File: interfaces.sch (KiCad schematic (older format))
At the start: 86 parts, among them IC3 TPD8S009DSMR, J4 WE_629105150521, J6 685119134923, J7 1140084168, Q2 BSS138APW, Q3 BSS138APW, Q4 BSS138APW, Q5 BSS138APW, Q6 BSS138APW, U7 FT4232HQ, U8 SRST, Y2 ABM8G-12.000MHZ-18-D2Y-T

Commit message: Update component library
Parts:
- C10: footprint antmicro-footprints:0603-cap -> lpddr4-test-board-footprints:0603-cap; symbol antmicroCapacitors0603:C_1u_0603 -> lpddr4-test-board:C_1u_0603
- Q2, Q3, Q4, Q5, Q6: footprint antmicro-footprints:SC70-3 -> lpddr4-test-board-footprints:SC70-3; symbol antmicroTransistorsFETsMOSFETsSingle:BSS138APW -> lpddr4-test-board:BSS138APW
- R1, R18, R19, R2, R20, R25, R3, R37, R4, R5, R6, R7, R8: footprint antmicro-footprints:0402-res -> lpddr4-test-board-footprints:0402-res; symbol antmicroResistors0402:R_22R_0402 -> lpddr4-test-board:R_22R_0402
- U7: footprint antmicro-footprints:FT4232HQ -> lpddr4-test-board-footprints:FT4232HQ; symbol antmicroInterfaceControllers:FT4232HQ -> lpddr4-test-board:FT4232HQ
- U8: symbol antmicroTestPoints:test -> lpddr4-test-board:test
- Y2: footprint antmicro-footprints:KX-7 -> lpddr4-test-board-footprints:KX-7; symbol antmicroCrystals:ABM8G-12.000MHZ-18-D2Y-T -> lpddr4-test-board:ABM8G-12.000MHZ-18-D2Y-T
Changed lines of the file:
@@
 User LEDs
 $Comp
-L antmicroTransistorsFETsMOSFETsSingle:BSS138APW Q2
+L lpddr4-test-board:BSS138APW Q2
 U 1 1 6090FD8D
 P 8300 8825
 F 0 "Q2" V 8567 8825 60  0000 C CNN
 F 1 "BSS138APW" V 8461 8825 60  0000 C CNN
-F 2 "antmicro-footprints:SC70-3" H 8500 9025 60  0001 L CNN
+F 2 "lpddr4-test-board-footprints:SC70-3" H 8500 9025 60  0001 L CNN
 F 3 "" H 8500 9125 60  0001 L CNN
 F 4 "BSS138PW" H 8500 9325 60  0001 L CNN "MPN"
@@
 $EndComp
 $Comp
-L antmicroTransistorsFETsMOSFETsSingle:BSS138APW Q4
+L lpddr4-test-board:BSS138APW Q4
 U 1 1 6091F8AC
 P 8325 9600
 F 0 "Q4" V 8592 9600 60  0000 C CNN
 F 1 "BSS138APW" V 8486 9600 60  0000 C CNN
-F 2 "antmicro-footprints:SC70-3" H 8525 9800 60  0001 L CNN
+F 2 "lpddr4-test-board-footprints:SC70-3" H 8525 9800 60  0001 L CNN
 F 3 "" H 8525 9900 60  0001 L CNN
 F 4 "BSS138PW" H 8525 10100 60  0001 L CNN "MPN"
@@
 $EndComp
 $Comp
-L antmicroTransistorsFETsMOSFETsSingle:BSS138APW Q5
+L lpddr4-test-board:BSS138APW Q5
 U 1 1 6092108D
 P 10475 8825
 F 0 "Q5" V 10742 8825 60  0000 C CNN
 F 1 "BSS138APW" V 10636 8825 60  0000 C CNN
-F 2 "antmicro-footprints:SC70-3" H 10675 9025 60  0001 L CNN
+F 2 "lpddr4-test-board-footprints:SC70-3" H 10675 9025 60  0001 L CNN
 F 3 "" H 10675 9125 60  0001 L CNN
 F 4 "BSS138PW" H 10675 9325 60  0001 L CNN "MPN"
@@
 $EndComp
 $Comp
-L antmicroTransistorsFETsMOSFETsSingle:BSS138APW Q6
+L lpddr4-test-board:BSS138APW Q6
 U 1 1 60922535
 P 10475 9600
 F 0 "Q6" V 10742 9600 60  0000 C CNN
 F 1 "BSS138APW" V 10636 9600 60  0000 C CNN
-F 2 "antmicro-footprints:SC70-3" H 10675 9800 60  0001 L CNN
+F 2 "lpddr4-test-board-footprints:SC70-3" H 10675 9800 60  0001 L CNN
 F 3 "" H 10675 9900 60  0001 L CNN
 F 4 "BSS138PW" H 10675 10100 60  0001 L CNN "MPN"
@@
 $EndComp
 $Comp
-L antmicroTransistorsFETsMOSFETsSingle:BSS138APW Q3
+L lpddr4-test-board:BSS138APW Q3
 U 1 1 60923B88
 P 8300 10375
 F 0 "Q3" V 8567 10375 60  0000 C CNN
 F 1 "BSS138APW" V 8461 10375 60  0000 C CNN
-F 2 "antmicro-footprints:SC70-3" H 8500 10575 60  0001 L CNN
+F 2 "lpddr4-test-board-footprints:SC70-3" H 8500 10575 60  0001 L CNN
 F 3 "" H 8500 10675 60  0001 L CNN
 F 4 "BSS138PW" H 8500 10875 60  0001 L CNN "MPN"
@@
 SD_DAT3
 $Comp
-L antmicroCapacitors0603:C_1u_0603 C10
+L lpddr4-test-board:C_1u_0603 C10
 U 1 1 617CD12F
 P 13300 8075
 F 0 "C10" H 13415 8120 60  0000 L CNN
 F 1 "C_1u_0603" H 13300 7925 60  0001 C CNN
-F 2 "antmicro-footprints:0603-cap" H 13500 8275 60  0001 L CNN
+F 2 "lpddr4-test-board-footprints:0603-cap" H 13500 8275 60  0001 L CNN
 F 3 "" H 13300 8075 50  0001 C CNN
 F 4 "WALSIN" H 13500 8475 60  0001 L CNN "Manufacturer"
@@
 User buttons
 $Comp
-L antmicroResistors0402:R_22R_0402 R18
+L lpddr4-test-board:R_22R_0402 R18
 U 1 1 6013A2FD
 P 5600 3000
 F 0 "R18" H 5800 3050 60  0000 C CNN
 F 1 "R_22R_0402" H 5600 2850 60  0001 C CNN
-F 2 "antmicro-footprints:0402-res" H 5800 3200 60  0001 L CNN
+F 2 "lpddr4-test-board-footprints:0402-res" H 5800 3200 60  0001 L CNN
 F 3 "" H 5600 3000 50  0001 C CNN
 F 4 "VISHAY" H 5800 3400 60  0001 L CNN "Manufacturer"
@@
 $EndComp
 $Comp
-L antmicroResistors0402:R_22R_0402 R19
+L lpddr4-test-board:R_22R_0402 R19
 U 1 1 6013A700
 P 5600 3100
 F 0 "R19" H 5800 3150 60  0000 C CNN
 F 1 "R_22R_0402" H 5600 2950 60  0001 C CNN
-F 2 "antmicro-footprints:0402-res" H 5800 3300 60  0001 L CNN
+F 2 "lpddr4-test-board-footprints:0402-res" H 5800 3300 60  0001 L CNN
 F 3 "" H 5600 3100 50  0001 C CNN
 F 4 "VISHAY" H 5800 3500 60  0001 L CNN "Manufacturer"
@@
 $EndComp
 $Comp
-L antmicroResistors0402:R_22R_0402 R20
+L lpddr4-test-board:R_22R_0402 R20
 U 1 1 6013A969
 P 5600 3200
 F 0 "R20" H 5800 3250 60  0000 C CNN
 F 1 "R_22R_0402" H 5600 3050 60  0001 C CNN
-F 2 "antmicro-footprints:0402-res" H 5800 3400 60  0001 L CNN
+F 2 "lpddr4-test-board-footprints:0402-res" H 5800 3400 60  0001 L CNN
 F 3 "" H 5600 3200 50  0001 C CNN
 F 4 "VISHAY" H 5800 3600 60  0001 L CNN "Manufacturer"
@@
 $EndComp
 $Comp
-L antmicroResistors0402:R_22R_0402 R25
+L lpddr4-test-board:R_22R_0402 R25
 U 1 1 6013AB72
 P 5600 3300
 F 0 "R25" H 5800 3350 60  0000 C CNN
 F 1 "R_22R_0402" H 5600 3150 60  0001 C CNN
-F 2 "antmicro-footprints:0402-res" H 5800 3500 60  0001 L CNN
+F 2 "lpddr4-test-board-footprints:0402-res" H 5800 3500 60  0001 L CNN
 F 3 "" H 5600 3300 50  0001 C CNN
 F 4 "VISHAY" H 5800 3700 60  0001 L CNN "Manufacturer"
@@
 	5150 3500 5500 3500
 $Comp
-L antmicroTestPoints:test U8
+L lpddr4-test-board:test U8
 U 1 1 601E16F4
 P 5700 3450
@@
 USR_BTN1
 $Comp
-L antmicroResistors0402:R_22R_0402 R1
+L lpddr4-test-board:R_22R_0402 R1
 U 1 1 5FE0DD48
 P 5600 3850
 F 0 "R1" H 5800 3900 60  0000 C CNN
 F 1 "R_22R_0402" H 5600 3700 60  0001 C CNN
-F 2 "antmicro-footprints:0402-res" H 5800 4050 60  0001 L CNN
+F 2 "lpddr4-test-board-footprints:0402-res" H 5800 4050 60  0001 L CNN
 F 3 "" H 5600 3850 50  0001 C CNN
 F 4 "VISHAY" H 5800 4250 60  0001 L CNN "Manufacturer"
@@
 $EndComp
 $Comp
-L antmicroResistors0402:R_22R_0402 R2
+L lpddr4-test-board:R_22R_0402 R2
 U 1 1 5FE0E0D9
 P 5600 3950
 F 0 "R2" H 5800 4000 60  0000 C CNN
 F 1 "R_22R_0402" H 5600 3800 60  0001 C CNN
-F 2 "antmicro-footprints:0402-res" H 5800 4150 60  0001 L CNN
+F 2 "lpddr4-test-board-footprints:0402-res" H 5800 4150 60  0001 L CNN
 F 3 "" H 5600 3950 50  0001 C CNN
 F 4 "VISHAY" H 5800 4350 60  0001 L CNN "Manufacturer"
@@
 $EndComp
 $Comp
-L antmicroResistors0402:R_22R_0402 R4
+L lpddr4-test-board:R_22R_0402 R4
 U 1 1 5FE0E52B
 P 5600 4150
 F 0 "R4" H 5800 4200 60  0000 C CNN
 F 1 "R_22R_0402" H 5600 4000 60  0001 C CNN
-F 2 "antmicro-footprints:0402-res" H 5800 4350 60  0001 L CNN
+F 2 "lpddr4-test-board-footprints:0402-res" H 5800 4350 60  0001 L CNN
 F 3 "" H 5600 4150 50  0001 C CNN
 F 4 "VISHAY" H 5800 4550 60  0001 L CNN "Manufacturer"
@@
 $EndComp
 $Comp
-L antmicroResistors0402:R_22R_0402 R3
+L lpddr4-test-board:R_22R_0402 R3
 U 1 1 5FE0E30A
 P 5600 4050
 F 0 "R3" H 5800 4100 60  0000 C CNN
 F 1 "R_22R_0402" H 5600 3900 60  0001 C CNN
-F 2 "antmicro-footprints:0402-res" H 5800 4250 60  0001 L CNN
+F 2 "lpddr4-test-board-footprints:0402-res" H 5800 4250 60  0001 L CNN
 F 3 "" H 5600 4050 50  0001 C CNN
 F 4 "VISHAY" H 5800 4450 60  0001 L CNN "Manufacturer"
@@
 UART1_RX
 $Comp
-L antmicroResistors0402:R_22R_0402 R6
+L lpddr4-test-board:R_22R_0402 R6
 U 1 1 5FEB07CF
 P 5600 4700
 F 0 "R6" H 5800 4750 60  0000 C CNN
 F 1 "R_22R_0402" H 5600 4550 60  0001 C CNN
-F 2 "antmicro-footprints:0402-res" H 5800 4900 60  0001 L CNN
+F 2 "lpddr4-test-board-footprints:0402-res" H 5800 4900 60  0001 L CNN
 F 3 "" H 5600 4700 50  0001 C CNN
 F 4 "VISHAY" H 5800 5100 60  0001 L CNN "Manufacturer"
@@
 $EndComp
 $Comp
-L antmicroResistors0402:R_22R_0402 R37
+L lpddr4-test-board:R_22R_0402 R37
 U 1 1 5FEB0AF8
 P 5600 5650
 F 0 "R37" H 5800 5700 60  0000 C CNN
 F 1 "R_22R_0402" H 5600 5500 60  0001 C CNN
-F 2 "antmicro-footprints:0402-res" H 5800 5850 60  0001 L CNN
+F 2 "lpddr4-test-board-footprints:0402-res" H 5800 5850 60  0001 L CNN
 F 3 "" H 5600 5650 50  0001 C CNN
 F 4 "VISHAY" H 5800 6050 60  0001 L CNN "Manufacturer"
@@
 UART1_TX
 $Comp
-L antmicroResistors0402:R_22R_0402 R7
+L lpddr4-test-board:R_22R_0402 R7
 U 1 1 5FEB126C
 P 5600 4800
 F 0 "R7" H 5800 4850 60  0000 C CNN
 F 1 "R_22R_0402" H 5600 4650 60  0001 C CNN
-F 2 "antmicro-footprints:0402-res" H 5800 5000 60  0001 L CNN
+F 2 "lpddr4-test-board-footprints:0402-res" H 5800 5000 60  0001 L CNN
 F 3 "" H 5600 4800 50  0001 C CNN
 F 4 "VISHAY" H 5800 5200 60  0001 L CNN "Manufacturer"
@@
 $EndComp
 $Comp
-L antmicroResistors0402:R_22R_0402 R8
+L lpddr4-test-board:R_22R_0402 R8
 U 1 1 5FEB1585
 P 5600 5550
 F 0 "R8" H 5800 5600 60  0000 C CNN
 F 1 "R_22R_0402" H 5600 5400 60  0001 C CNN
-F 2 "antmicro-footprints:0402-res" H 5800 5750 60  0001 L CNN
+F 2 "lpddr4-test-board-footprints:0402-res" H 5800 5750 60  0001 L CNN
 F 3 "" H 5600 5550 50  0001 C CNN
 F 4 "VISHAY" H 5800 5950 60  0001 L CNN "Manufacturer"
@@
 AUX_JTAG_TCK
 $Comp
-L antmicroResistors0402:R_22R_0402 R5
+L lpddr4-test-board:R_22R_0402 R5
 U 1 1 601136B0
 P 5600 4350
 F 0 "R5" H 5800 4400 60  0000 C CNN
 F 1 "R_22R_0402" H 5600 4200 60  0001 C CNN
-F 2 "antmicro-footprints:0402-res" H 5800 4550 60  0001 L CNN
+F 2 "lpddr4-test-board-footprints:0402-res" H 5800 4550 60  0001 L CNN
 F 3 "" H 5600 4350 50  0001 C CNN
 F 4 "VISHAY" H 5800 4750 60  0001 L CNN "Manufacturer"
@@
 	3550 6800 3550 7350
 $Comp
-L antmicroInterfaceControllers:FT4232HQ U7
+L lpddr4-test-board:FT4232HQ U7
 U 1 1 601044E5
 P 4350 5150
 F 0 "U7" H 4350 7637 60  0000 C CNN
 F 1 "FT4232HQ" H 4350 7531 60  0000 C CNN
-F 2 "antmicro-footprints:FT4232HQ" V 4550 5350 60  0001 L CNN
+F 2 "lpddr4-test-board-footprints:FT4232HQ" V 4550 5350 60  0001 L CNN
 F 3 "https://www.ftdichip.com/Support/Documents/DataSheets/ICs/DS_FT4232H.pdf" H 4550 5550 60  0001 L CNN
 F 4 "FTDI" H 4550 6300 60  0001 L CNN "Manufacturer"
@@
 3V3_SYS
 $Comp
-L antmicroCrystals:ABM8G-12.000MHZ-18-D2Y-T Y2
+L lpddr4-test-board:ABM8G-12.000MHZ-18-D2Y-T Y2
 U 1 1 61D2EA50
 P 2875 6550
 F 0 "Y2" H 3069 6643 31  0000 L CNN
 F 1 "ABM8G-12.000MHZ-18-D2Y-T" H 3069 6581 31  0000 L CNN
-F 2 "antmicro-footprints:KX-7" H 4975 6550 50  0001 C CNN
+F 2 "lpddr4-test-board-footprints:KX-7" H 4975 6550 50  0001 C CNN
 F 3 "" H 5075 6650 50  0001 C CNN
 F 4 "ABM8G-12.000MHZ-18-D2Y-T " H 3069 6519 31  0000 L CNN "MPN"

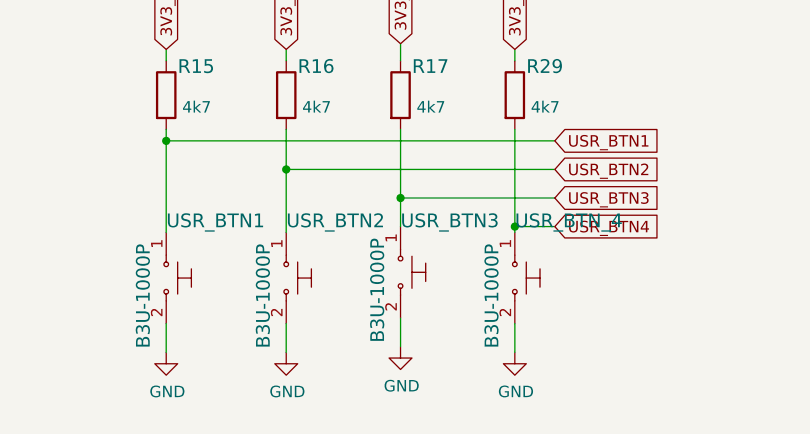
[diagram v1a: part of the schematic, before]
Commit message: Cleaned up designators
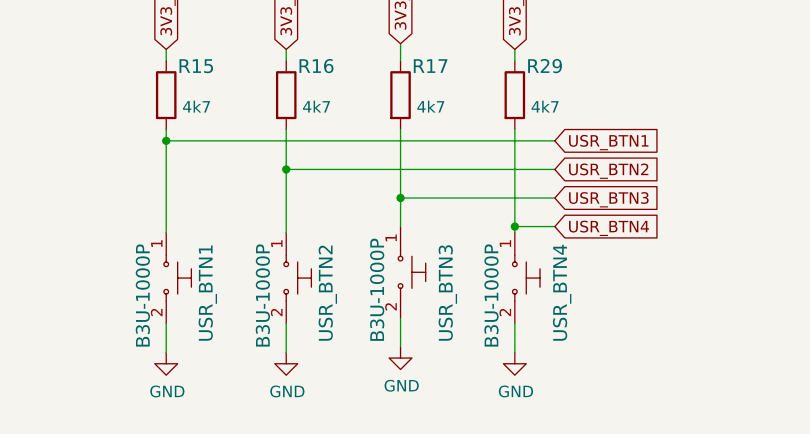
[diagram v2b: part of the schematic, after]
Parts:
- renumbered USR_BTN_4 to USR_BTN4
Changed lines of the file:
@@
 AR Path="/5FD53C7D/5FCEBF82" Ref="PROG_B?"  Part="1"
 AR Path="/600E76D8/5FCEBF82" Ref="USR_BTN2"  Part="1"
-F 0 "USR_BTN2" V 4125 10125 60  0000 L CNN
+F 0 "USR_BTN2" H 4225 10300 60  0000 L CNN
 F 1 "B3U-1000P" H 4225 10025 60  0000 L CNN
 F 2 "lpddr4-test-board-footprints:Switch_Tactile_SMD_B3U-1000P" H 4575 10325 60  0001 L CNN
@@
 AR Path="/5FD53C7D/5FDD28F9" Ref="PROG_B?"  Part="1"
 AR Path="/600E76D8/5FDD28F9" Ref="USR_BTN1"  Part="1"
-F 0 "USR_BTN1" V 3600 10125 60  0000 L CNN
+F 0 "USR_BTN1" H 3700 10300 60  0000 L CNN
 F 1 "B3U-1000P" H 3700 10025 60  0000 L CNN
 F 2 "lpddr4-test-board-footprints:Switch_Tactile_SMD_B3U-1000P" H 4050 10325 60  0001 L CNN
@@
 AR Path="/5FD53C7D/5FE766D1" Ref="PROG_B?"  Part="1"
 AR Path="/600E76D8/5FE766D1" Ref="USR_BTN3"  Part="1"
-F 0 "USR_BTN3" V 4650 10100 60  0000 L CNN
+F 0 "USR_BTN3" H 4750 10300 60  0000 L CNN
 F 1 "B3U-1000P" H 4725 10000 60  0000 L CNN
 F 2 "lpddr4-test-board-footprints:Switch_Tactile_SMD_B3U-1000P" H 5075 10300 60  0001 L CNN
@@
 P 5375 10125
 AR Path="/5FD53C7D/5FCB7E4F" Ref="PROG_B?"  Part="1"
-AR Path="/600E76D8/5FCB7E4F" Ref="USR_BTN_4"  Part="1"
-F 0 "USR_BTN_4" V 5125 10125 60  0000 L CNN
+AR Path="/600E76D8/5FCB7E4F" Ref="USR_BTN4"  Part="1"
+F 0 "USR_BTN4" H 5225 10325 60  0000 L CNN
 F 1 "B3U-1000P" H 5225 10025 60  0000 L CNN
 F 2 "lpddr4-test-board-footprints:Switch_Tactile_SMD_B3U-1000P" H 5575 10325 60  0001 L CNN
